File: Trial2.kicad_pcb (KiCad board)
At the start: 2 copper layers, 3 parts, among them J1 Barrel_Jack_Switch

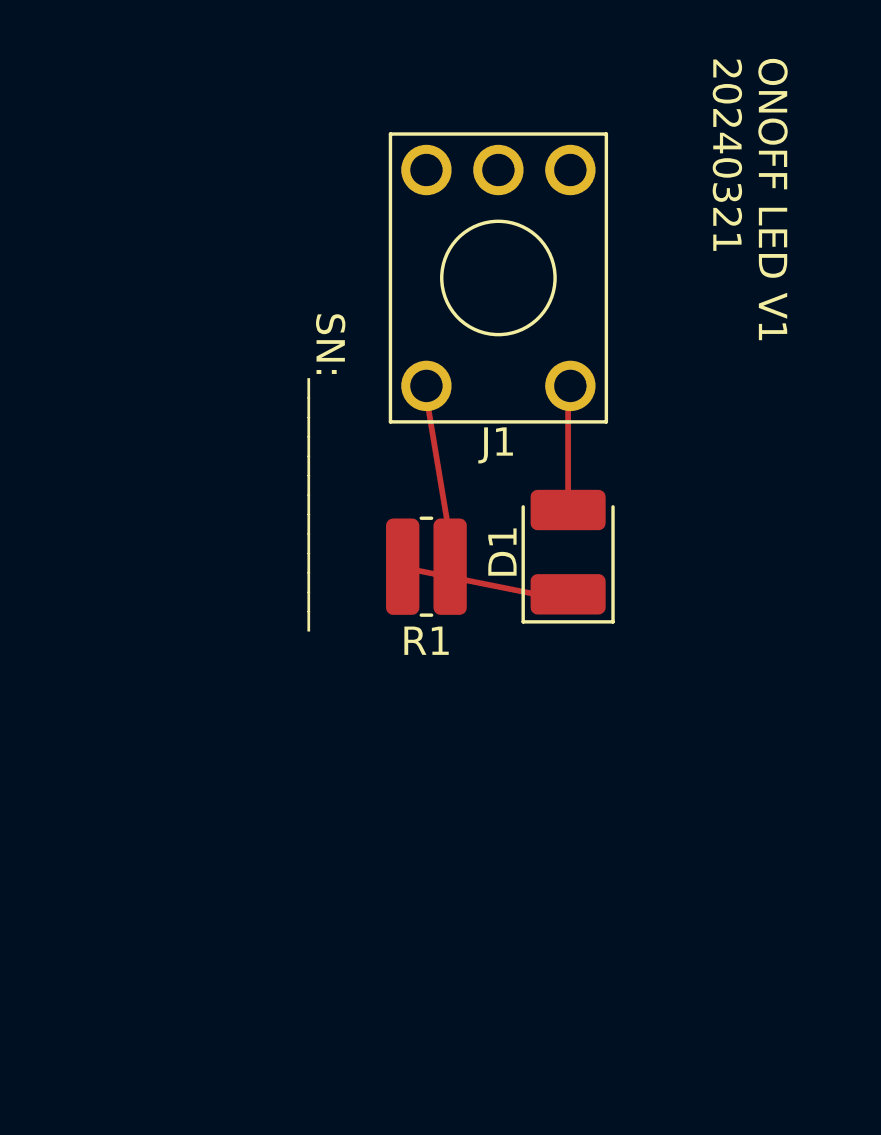
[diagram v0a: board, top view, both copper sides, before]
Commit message: Circuit Edits
I added a Molex connector 01x03 and a Switch
I added footprints for the connector and the Switch
I added the sheet info
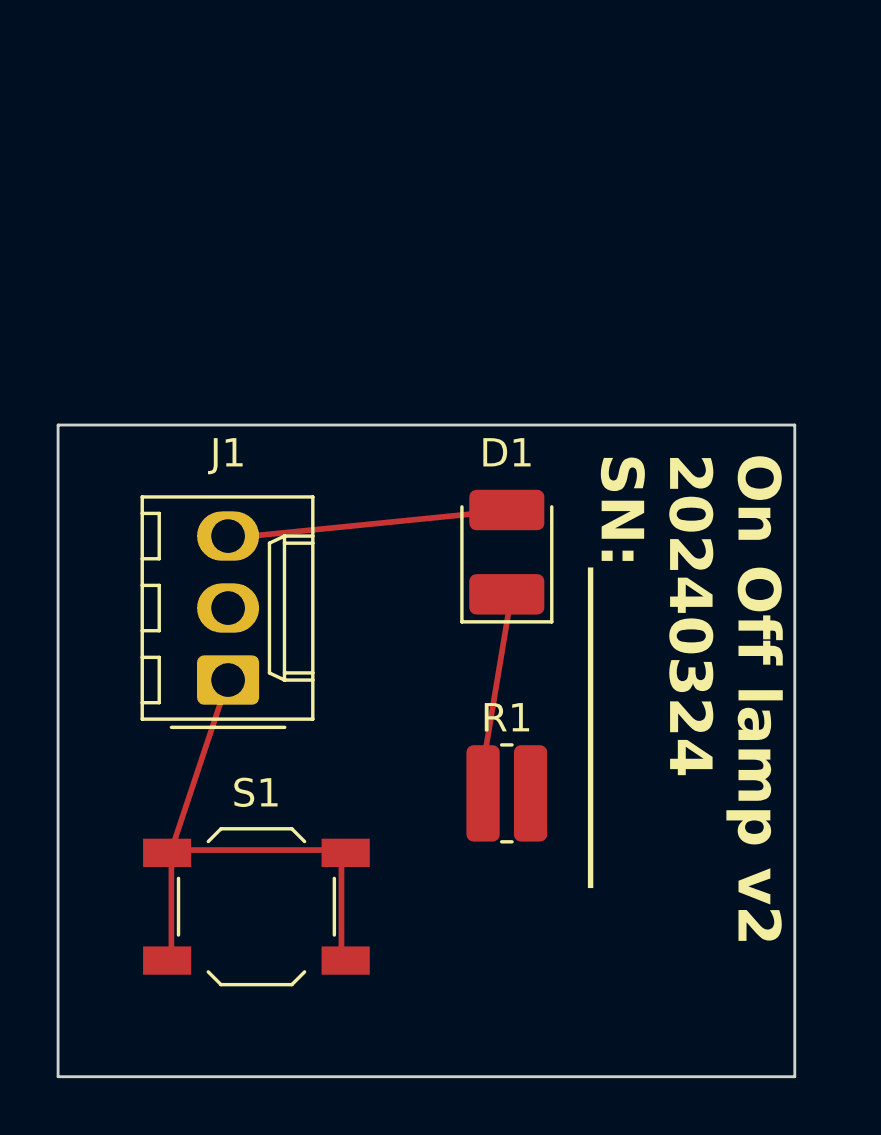
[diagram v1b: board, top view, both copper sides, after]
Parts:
- added S1: SWITCH_TACTILE_SPST-NO_0.05A_24V, Button_Switch_SMD:SW_SPST_TL3342, F.Cu at (134.0, 119.0)
- J1: value Barrel_Jack_Switch -> Conn_01x03; footprint Button_Switch_THT:KSA_Tactile_SPST -> Connector_Molex:Molex_KK-254_AE-6410-03A_1x03_P2.54mm_Vertical
- moved J1 15.9 mm to (133.0, 111.0), turned to 90 degrees
- moved R1 8.49 mm to (142.8, 115.0), turned to 0 degrees
- moved D1 2.16 mm to (142.8, 106.5)
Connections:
- D1 pad 2: Net-(D1-A) -> +3.3V
- J1 pad 1: Net-(D1-A) -> Net-(J1-Pin_1)
- J1 pad 2: unconnected-(J1-Pad2) -> GND
- J1 pad 3: Net-(J1-Pad3) -> +3.3V
- R1 pad 1: Net-(J1-Pad3) -> Net-(D1-K)
- R1 pad 2: Net-(D1-K) -> GND
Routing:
- added copper zone on F.Cu, net GND
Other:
- board outline added: 26 x 23 mm
- board text added: "On Off lamp v2 20240324 SN:___________"
- board text removed: "ONOFF LED V1 20240321"
- board text removed: "SN:_____________"

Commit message: No further edits
This project is on pause as is until further notice.
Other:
- board size 26 x 23 mm -> 27 x 23 mm
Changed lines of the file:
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@@
   )
   (paper "A4")
+  (title_block
+    (title "On Off switch ")
+    (date "2024-03-26")
+    (rev "V2")
+    (company "PubInv")
+    (comment 1 "Volunteering ")
+    (comment 2 "Mentorred by Forest Lee Ereckson ")
+  )
   (layers
     (0 "F.Cu" signal)
@@
     (pcbplotparams
       (layerselection 0x00010fc_ffffffff)
-      (plot_on_all_layers_selection 0x0000000_00000000)
+      (plot_on_all_layers_selection 0x0000020_00000001)
       (disableapertmacros false)
       (usegerberextensions false)
@@
       (outputformat 1)
       (mirror false)
-      (drillshape 1)
+      (drillshape 0)
       (scaleselection 1)
       (outputdirectory "")
@@
     (fp_line (start 1.6 1.25) (end 1.6 -1.25)
       (stroke (width 0.1) (type solid)) (layer "F.Fab"))
-    (pad "1" smd roundrect (at -1.4875 0 90) (size 1.425 2.65) (layers "F.Cu" "F.Paste" "F.Mask") (roundrect_rratio 0.175439)
+    (pad "1" smd roundrect (at -1.4875 0 90) (size 1.425 2.65) (layers "F.Cu" "F.Paste" "F.Mask") (roundrect_rratio 0.1754392982)
       (net 1 "Net-(D1-K)") (pinfunction "K") (pintype "passive"))
-    (pad "2" smd roundrect (at 1.4875 0 90) (size 1.425 2.65) (layers "F.Cu" "F.Paste" "F.Mask") (roundrect_rratio 0.175439)
+    (pad "2" smd roundrect (at 1.4875 0 90) (size 1.425 2.65) (layers "F.Cu" "F.Paste" "F.Mask") (roundrect_rratio 0.1754392982)
       (net 2 "+3.3V") (pinfunction "A") (pintype "passive"))
     (model "${KICAD6_3DMODEL_DIR}/LED_SMD.3dshapes/LED_1210_3225Metric.wrl"
@@
     (fp_line (start 6.35 2.88) (end 6.35 -2.92)
       (stroke (width 0.1) (type solid)) (layer "F.Fab"))
-    (pad "1" thru_hole roundrect (at 0 0 90) (size 1.74 2.19) (drill 1.19) (layers "*.Cu" "*.Mask") (roundrect_rratio 0.143678)
+    (pad "1" thru_hole roundrect (at 0 0 90) (size 1.74 2.19) (drill 1.19) (layers "*.Cu" "*.Mask") (roundrect_rratio 0.1436781609)
       (net 4 "Net-(J1-Pin_1)") (pinfunction "Pin_1") (pintype "passive"))
     (pad "2" thru_hole oval (at 2.54 0 90) (size 1.74 2.19) (drill 1.19) (layers "*.Cu" "*.Mask")
@@
     (fp_line (start 0.8 1.6) (end -0.8 1.6)
       (stroke (width 0.1) (type solid)) (layer "F.Fab"))
-    (pad "1" smd roundrect (at -0.8375 0) (size 1.175 3.4) (layers "F.Cu" "F.Paste" "F.Mask") (roundrect_rratio 0.212766)
+    (pad "1" smd roundrect (at -0.8375 0) (size 1.175 3.4) (layers "F.Cu" "F.Paste" "F.Mask") (roundrect_rratio 0.2127659574)
       (net 1 "Net-(D1-K)") (pintype "passive"))
-    (pad "2" smd roundrect (at 0.8375 0) (size 1.175 3.4) (layers "F.Cu" "F.Paste" "F.Mask") (roundrect_rratio 0.212766)
+    (pad "2" smd roundrect (at 0.8375 0) (size 1.175 3.4) (layers "F.Cu" "F.Paste" "F.Mask") (roundrect_rratio 0.2127659574)
       (net 3 "GND") (pintype "passive"))
     (model "${KICAD6_3DMODEL_DIR}/Resistor_SMD.3dshapes/R_0612_1632Metric.wrl"
@@
   (gr_line (start 137 117) (end 131 117)
     (stroke (width 0.2) (type default)) (layer "F.Cu"))
-  (gr_rect (start 127 102) (end 153 125)
+  (gr_rect (start 127 102) (end 154 125)
     (stroke (width 0.1) (type default)) (fill none) (layer "Edge.Cuts"))
   (gr_text "On Off lamp v2\n20240324\nSN:___________" (at 146 103 -90) (layer "F.SilkS")
@@
       (pts
         (xy 127 102)
-        (xy 153 102)
-        (xy 153 125)
+        (xy 154 102)
+        (xy 154 125)
         (xy 127 125)
         (xy 127 123)
